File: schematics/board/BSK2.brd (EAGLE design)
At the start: 82 x 100 mm, 18 parts

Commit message: Новые схемы
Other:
- board text added: "BSK2 "Концерн ИТС""
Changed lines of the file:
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@@
 <text x="59.4" y="33.1" size="1.4224" layer="26" rot="MR0">BUS-</text>
 <text x="26.9" y="33.1" size="1.4224" layer="26" rot="MR0">BUS-</text>
+<text x="13.8" y="67.9" size="1.4224" layer="25" rot="MR45">BUS+</text>
+<text x="72.2" y="72" size="1.4224" layer="26" rot="MR315">BUS+</text>
+<text x="60.2" y="23.4" size="1.4224" layer="26" rot="MR225">BUS+</text>
+<text x="17.6" y="19.3" size="1.4224" layer="26" rot="MR135">BUS+</text>
+<text x="22.6" y="59.3" size="1.4224" layer="26" rot="MR45">BUS-</text>
+<text x="62.1" y="62.1" size="1.4224" layer="26" rot="MR315">BUS-</text>
+<text x="52.2" y="31.5" size="1.4224" layer="26" rot="MR225">BUS-</text>
+<text x="26.1" y="27.8" size="1.4224" layer="26" rot="MR135">BUS-</text>
+<text x="81" y="40.1" size="1.778" layer="25" rot="R90">BSK2 "Концерн ИТС"</text>
 </plain>
 <attributes>

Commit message: изменен БСК4
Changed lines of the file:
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@@
 <text x="59.4" y="33.1" size="1.4224" layer="26" rot="MR0">BUS-</text>
 <text x="26.9" y="33.1" size="1.4224" layer="26" rot="MR0">BUS-</text>
-<text x="13.8" y="67.9" size="1.4224" layer="25" rot="MR45">BUS+</text>
+<text x="13.8" y="67.9" size="1.4224" layer="26" rot="MR45">BUS+</text>
 <text x="72.2" y="72" size="1.4224" layer="26" rot="MR315">BUS+</text>
 <text x="60.2" y="23.4" size="1.4224" layer="26" rot="MR225">BUS+</text>
@@
 <text x="52.2" y="31.5" size="1.4224" layer="26" rot="MR225">BUS-</text>
 <text x="26.1" y="27.8" size="1.4224" layer="26" rot="MR135">BUS-</text>
-<text x="81" y="40.1" size="1.778" layer="25" rot="R90">BSK2 "Концерн ИТС"</text>
+<text x="52.2" y="1.9" size="1.778" layer="26" rot="MR0">BSK2 "Концерн ИТС"</text>
 </plain>
 <attributes>

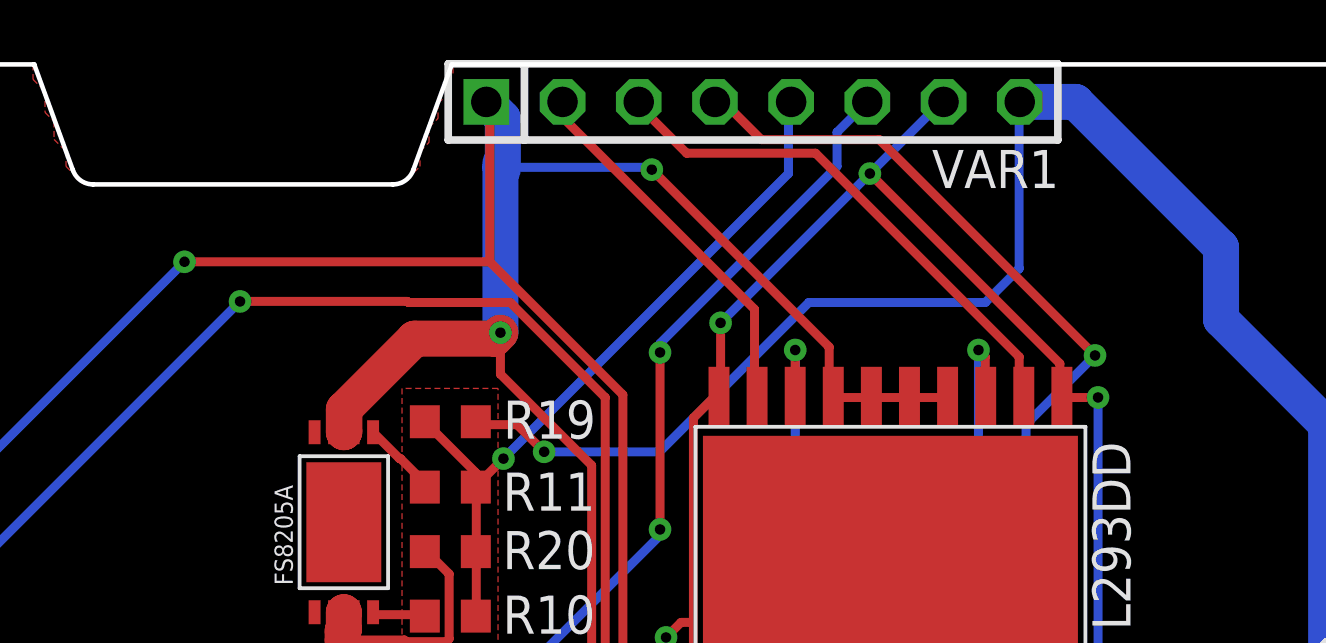
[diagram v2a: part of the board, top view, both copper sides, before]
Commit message: доработана схема БСК1
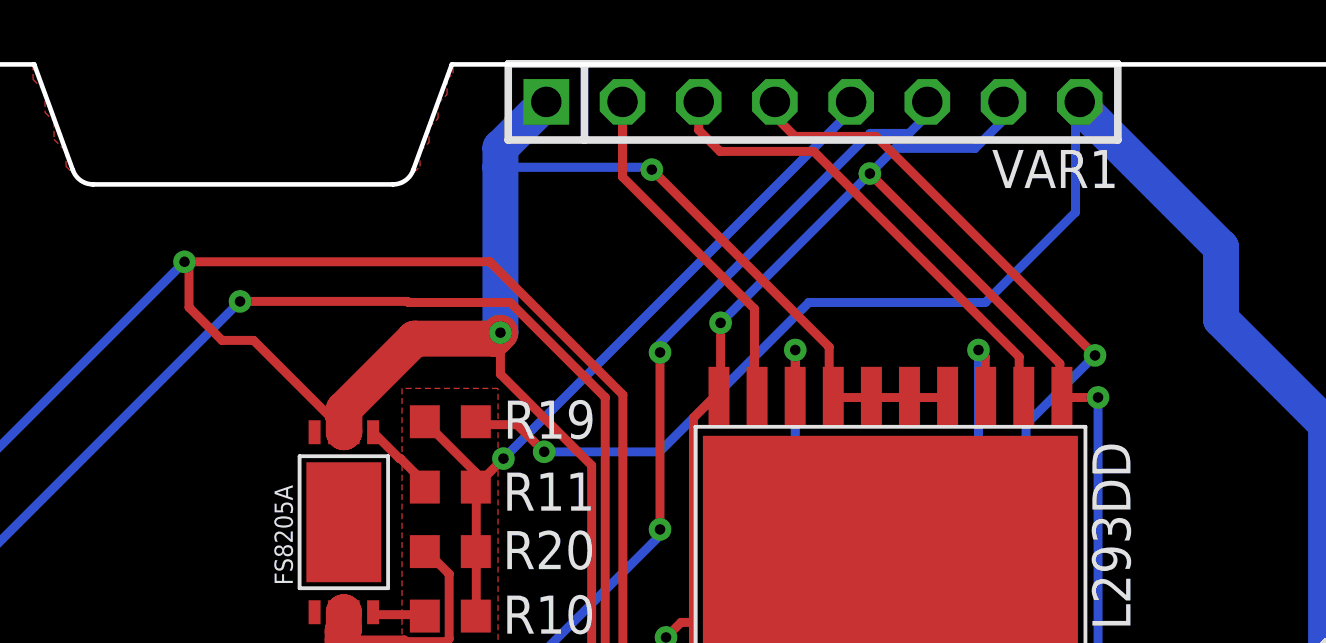
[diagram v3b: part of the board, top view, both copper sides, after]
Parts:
- moved VAR1 2.00 mm to (49.0, 98.8)
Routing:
- net GND: track 143.3 -> 146.3 mm
- net 5V: track 65.9 -> 68.2 mm
- net KHEAT1: track 32.0 -> 30.3 mm
- net KEM1: track 17.6 -> 16.1 mm
- net 1W: track 40.9 -> 42.3 mm
- net BUS+: track 71.2 -> 70.2 mm
- net KVCC1: track 24.4 -> 25.2 mm
- net KEM2: track 12.5 -> 11.7 mm

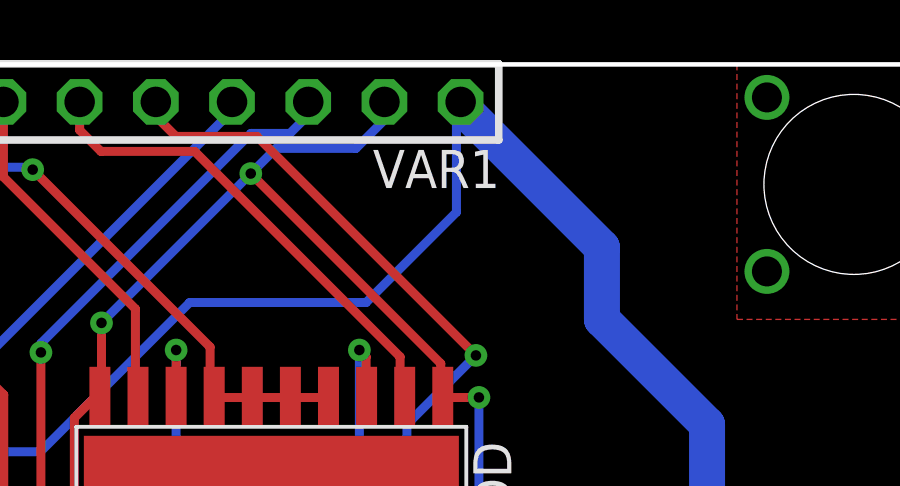
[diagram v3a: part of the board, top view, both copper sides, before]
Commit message: Реструктурированы сигналы коммутации для плат БСК
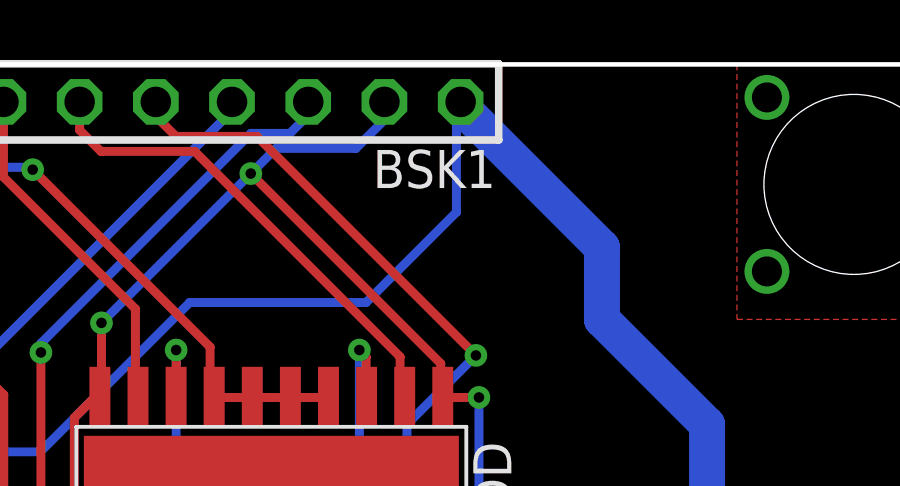
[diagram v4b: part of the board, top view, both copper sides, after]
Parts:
- renumbered VAR1 to BSK1
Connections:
- net KEM1 renamed B2_KEM+
- net KEM2 renamed B2_KEM-
- net KHEAT1 renamed B2_KHEAT
- net KVCC1 renamed B2_KVCC
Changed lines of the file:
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@@
 <attribute name="VALUE" x="23.310459375" y="27.30414375" size="1.27" layer="27" rot="R135"/>
 </element>
-<element name="VAR1" library="pinheadCS" package="1X08" value="" x="49" y="98.75" smashed="yes">
+<element name="BSK1" library="pinheadCS" package="1X08" value="" x="49" y="98.75" smashed="yes">
 <attribute name="NAME" x="54.9638" y="95.8788" size="1.27" layer="25" ratio="10"/>
 <attribute name="VALUE" x="38.84" y="95.575" size="1.27" layer="27"/>
@@
 <contactref element="U$8" pad="17"/>
 <contactref element="U$14" pad="67"/>
-<contactref element="VAR1" pad="1"/>
+<contactref element="BSK1" pad="1"/>
 <wire x1="33.36" y1="87.74" x2="33.3776" y2="87.7576" width="1.2" layer="1"/>
 <wire x1="33.3776" y1="88.2918" x2="33.3776" y2="87.7576" width="1.2" layer="1"/>
@@
 <contactref element="U$8" pad="11"/>
 <contactref element="U$8" pad="20"/>
-<contactref element="VAR1" pad="7"/>
+<contactref element="BSK1" pad="7"/>
 <contactref element="U$5" pad="3"/>
 <wire x1="57.295" y1="79.32" x2="57.4548" y2="79.3962" width="0.3" layer="1"/>
@@
 <signal name="1W">
 <contactref element="U$5" pad="4"/>
-<contactref element="VAR1" pad="6"/>
+<contactref element="BSK1" pad="6"/>
 <wire x1="35.88" y1="71.875" x2="35.005" y2="71" width="0.3" layer="1"/>
 <wire x1="35.005" y1="71" x2="33.7" y2="71" width="0.3" layer="1"/>
@@
 <wire x1="43.9" y1="90.7" x2="50.9" y2="97.7" width="0.3" layer="16"/>
 </signal>
-<signal name="KEM1">
-<contactref element="VAR1" pad="3"/>
+<signal name="B2_KEM+">
+<contactref element="BSK1" pad="3"/>
 <contactref element="U$8" pad="2"/>
 <wire x1="55.8714" y1="89.1228" x2="55.8714" y2="90.2538" width="0.3" layer="1"/>
@@
 <wire x1="55.8714" y1="90.2538" x2="49.0252" y2="97.1" width="0.3" layer="1"/>
 </signal>
-<signal name="KEM2">
-<contactref element="VAR1" pad="2"/>
+<signal name="B2_KEM-">
+<contactref element="BSK1" pad="2"/>
 <contactref element="U$8" pad="9"/>
 <wire x1="47.135" y1="88.92" x2="47.0496" y2="89.1228" width="0.3" layer="1"/>
@@
 <wire x1="47.0496" y1="91.8504" x2="42.65" y2="96.25" width="0.3" layer="1"/>
 </signal>
-<signal name="KHEAT1">
-<contactref element="VAR1" pad="4"/>
+<signal name="B2_KHEAT">
+<contactref element="BSK1" pad="4"/>
 <contactref element="U$8" pad="19"/>
 <wire x1="56.025" y1="79.32" x2="56.025" y2="77.475" width="0.3" layer="1"/>
@@
 <wire x1="19.010596875" y1="81.210596875" x2="29.9" y2="92.1" width="0.3" layer="16"/>
 </signal>
-<signal name="KVCC1">
-<contactref element="VAR1" pad="5"/>
+<signal name="B2_KVCC">
+<contactref element="BSK1" pad="5"/>
 <contactref element="R10" pad="1"/>
 <contactref element="R11" pad="1"/>
@@
 <signal name="BUS+">
 <contactref element="R19" pad="2"/>
-<contactref element="VAR1" pad="8"/>
+<contactref element="BSK1" pad="8"/>
 <contactref element="U$3" pad="1"/>
 <contactref element="U$3" pad="2"/>

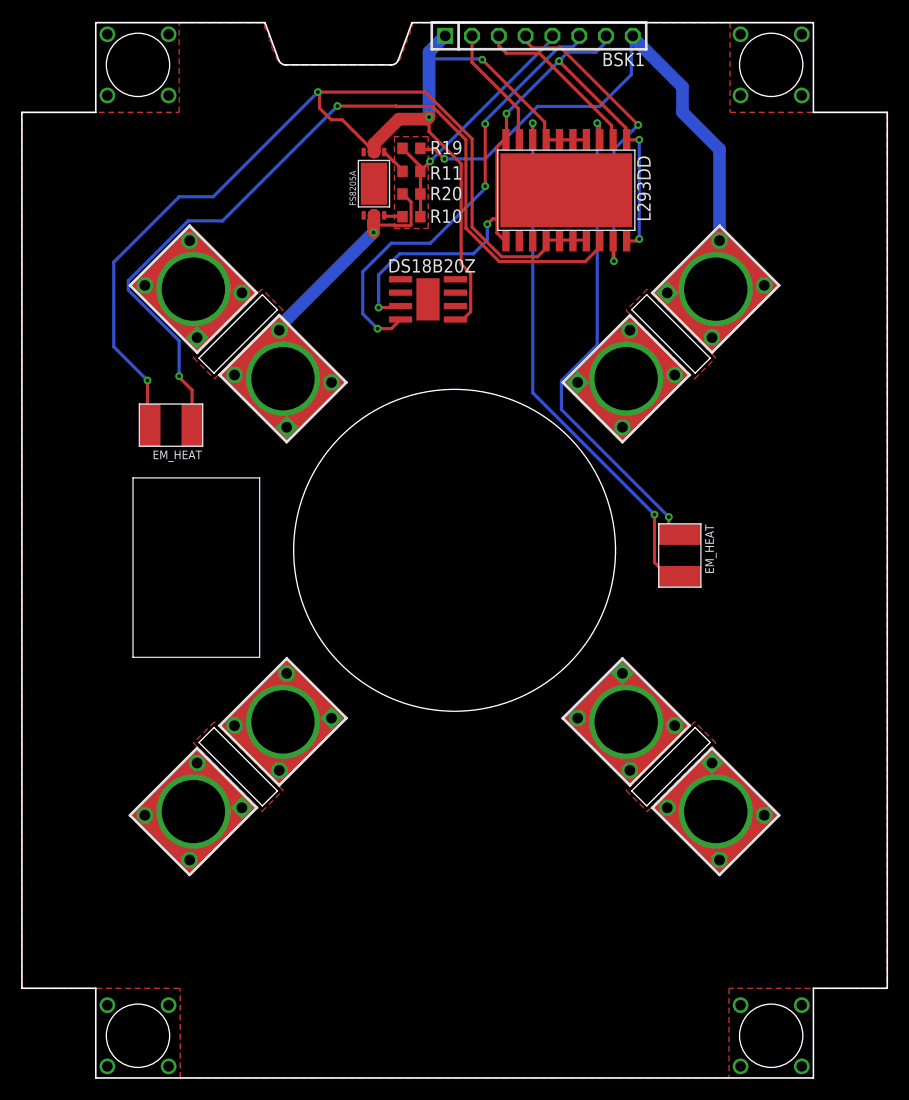
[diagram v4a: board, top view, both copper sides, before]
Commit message: Разведены платы БСК2-5
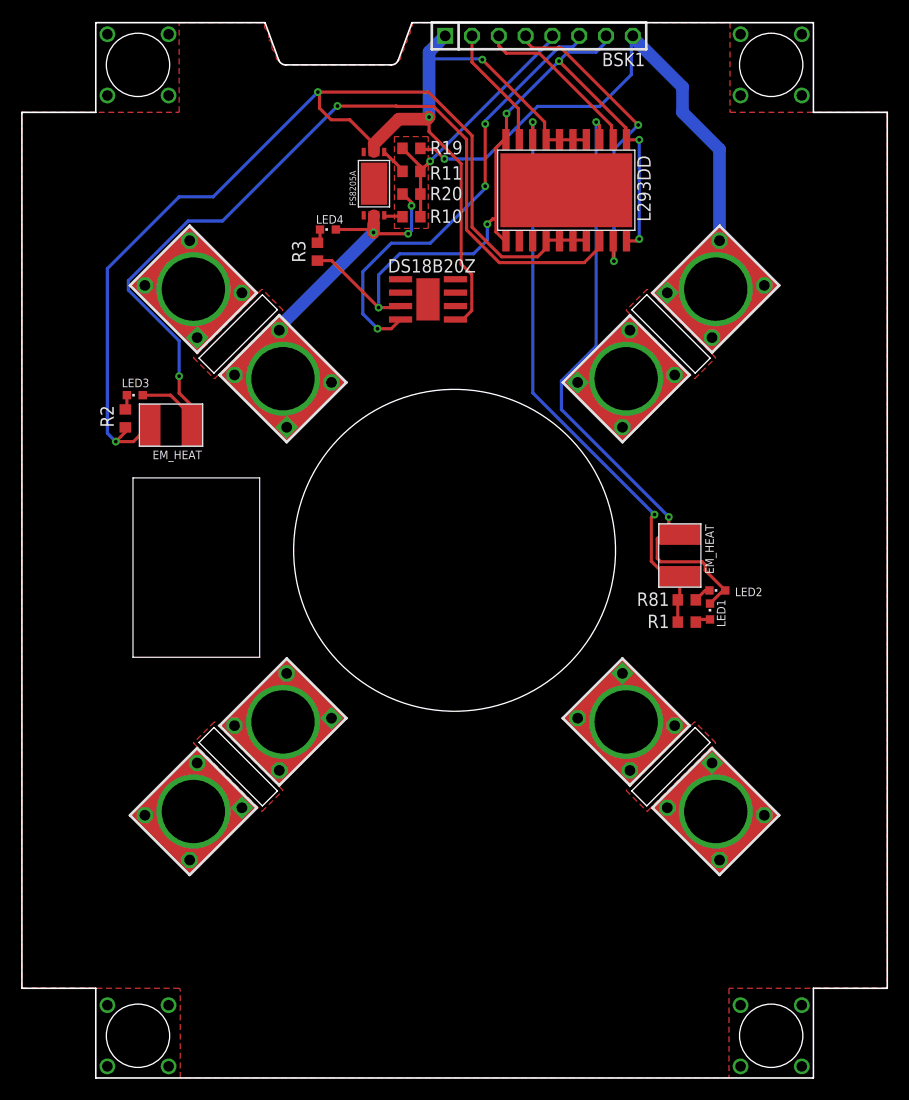
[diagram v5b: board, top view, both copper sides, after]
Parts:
- added LED1, LED2, LED3, LED4: (no value), led:CHIPLED_0603
- added R1, R2, R3, R81: 2k, resistor:R0603
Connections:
- new net N$22: LED2.C, R81.2
- new net N$23: LED1.A, R1.2
- new net N$24: LED3.C, R2.1
- new net N$25: LED4.C, R3.2
- net 5V: now also R3.1
- net BUS-: now also LED4.A
- net GND: now also R2.2
- net N$1: now also LED1.C, LED2.A
- net N$2: now also R1.1, R81.1
- net N$3: now also LED3.A
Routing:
- net N$1: track 46.7 -> 61.0 mm
- net 5V: track 68.2 -> 74.8 mm
- net N$3: track 80.1 -> 86.4 mm
- net GND: track 146.3 -> 151.7 mm
- net N$2: track 50.9 -> 55.9 mm
- net BUS-: track 40.4 -> 44.6 mm, vias 1 -> 3
- net N$22: track 0.00 -> 1.67 mm
- net N$23: track 0.00 -> 1.45 mm
- net N$24: track 0.00 -> 1.41 mm
- net N$25: track 0.00 -> 1.35 mm
- net BUS+: track 70.2 -> 69.5 mm
